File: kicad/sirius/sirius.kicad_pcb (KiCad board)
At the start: 4 copper layers, 42.1 x 65.5 mm, 60 parts, among them J1 IPEX_MHF1, J2 Power In, J3 Screw_Terminal, Q1 Q_PMOS_GSD, Q2 Q_NMOS_GSD, Q3 Q_NMOS_GSD, U1 Power_Connector, U2 AP63301WU-7, U3 RFM95W-915S2, U4 LC29H (DA), U5 Pi Zero 2W

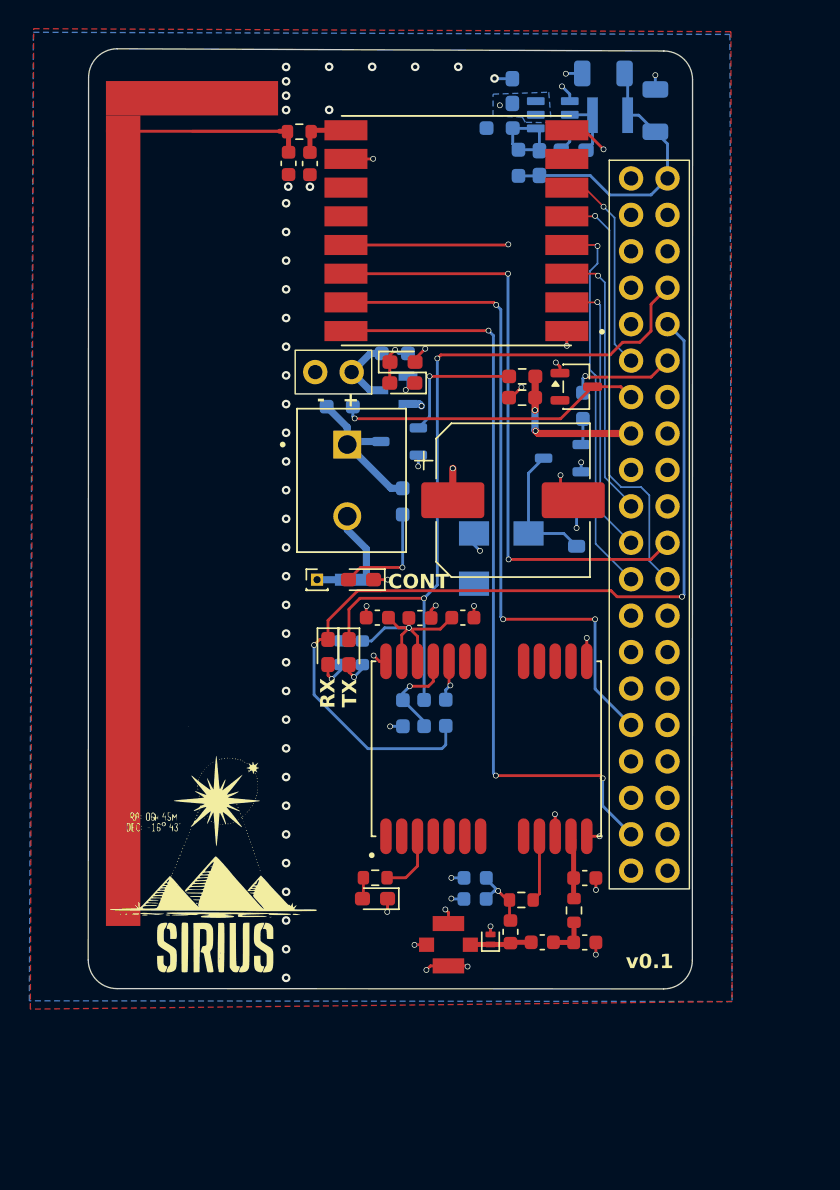
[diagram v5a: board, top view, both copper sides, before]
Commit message: WIP: Start making new version of Sirius
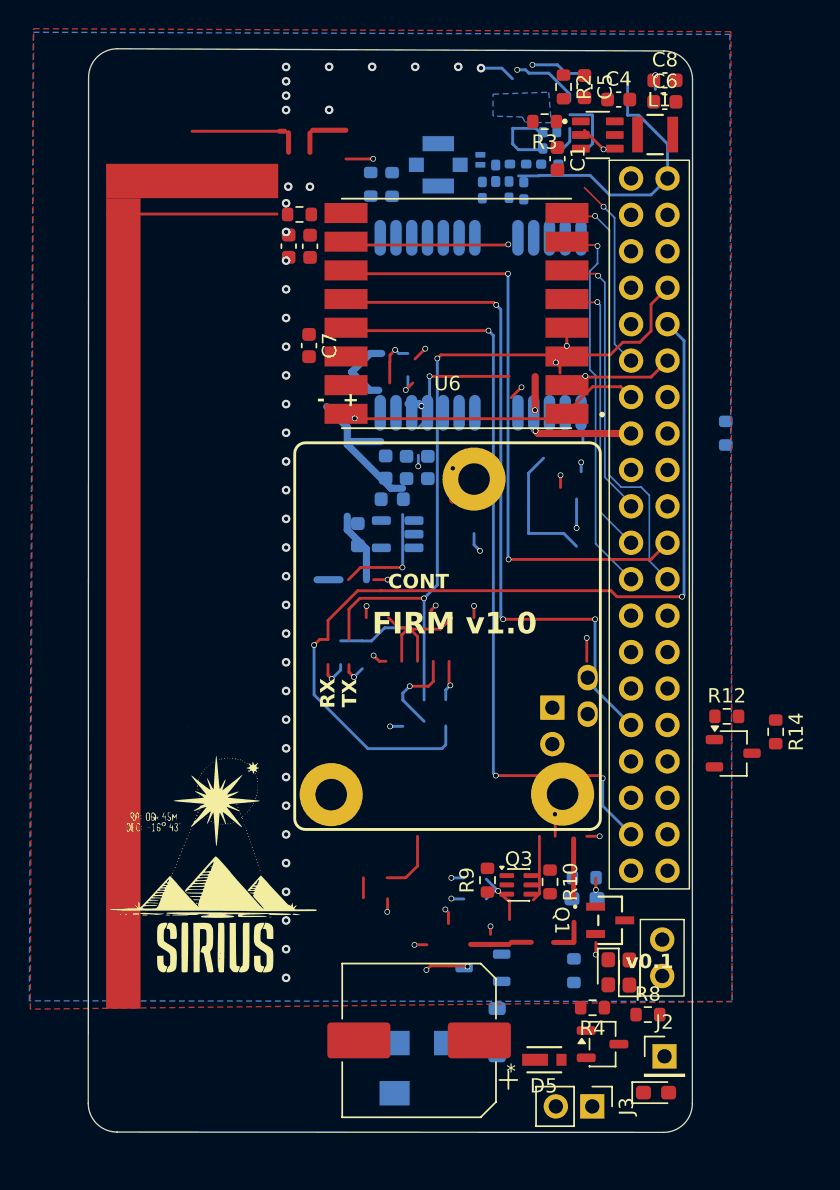
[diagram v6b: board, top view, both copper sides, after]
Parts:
- removed the D7 at (129.8, 108.4)
- removed the D8 at (131.2, 108.4)
- removed the R14 at (136.5, 112.6)
- removed the R16 at (132.2, 108.4)
- removed the R8 at (138.0, 112.6)
- added C14: 470p, Capacitor_SMD:C_0603_1608Metric, B.Cu at (131.9, 100.2)
- added C16: 10u, Capacitor_SMD:C_0603_1608Metric, B.Cu at (134.3, 97.7)
- added C8: 22u, Capacitor_SMD:C_0603_1608Metric, F.Cu at (153.3, 68.5)
- added Q3: Q_Dual_NMOS, Package_TO_SOT_SMD:SOT-363_SC-70-6, F.Cu at (143.1, 124.6)
- added R10: 10k, Resistor_SMD:R_0603_1608Metric, F.Cu at (145.3, 124.4)
- added R9: 10k, Resistor_SMD:R_0603_1608Metric, F.Cu at (140.9, 124.3)
- added U4: MIC5219-3.3YM5, Package_TO_SOT_SMD:SOT-23-5, B.Cu at (134.6, 100.1)
- added U6: ~, sirius:FIRM v1.0, F.Cu at (138.1, 107.6)
- C1, C4, C5: footprint Capacitor_SMD:C_0603_1608Metric_Pad1.08x0.95mm_HandSolder -> Capacitor_SMD:C_0603_1608Metric; moved to F.Cu
- C10: renamed from C9; footprint Capacitor_SMD:C_0603_1608Metric -> Capacitor_SMD:C_0402_1005Metric_Pad0.74x0.62mm_HandSolder; moved to B.Cu
- C11: renamed from C10; footprint Capacitor_SMD:C_0603_1608Metric -> Capacitor_SMD:C_0402_1005Metric_Pad0.74x0.62mm_HandSolder; moved to B.Cu
- C12: renamed from C11; footprint Capacitor_SMD:C_0603_1608Metric -> Capacitor_SMD:C_0402_1005Metric_Pad0.74x0.62mm_HandSolder; moved to B.Cu
- C13: renamed from C12; footprint Capacitor_SMD:C_0603_1608Metric -> Capacitor_SMD:C_0402_1005Metric_Pad0.74x0.62mm_HandSolder
- C15: renamed from C13; footprint Capacitor_SMD:C_0603_1608Metric -> Capacitor_SMD:C_0402_1005Metric_Pad0.74x0.62mm_HandSolder
- C17: renamed from C14; moved to B.Cu
- C18: renamed from C15; moved to B.Cu
- C19: renamed from C16; moved to B.Cu
- C6: footprint Capacitor_SMD:C_1206_3216Metric -> Capacitor_SMD:C_0603_1608Metric; moved to F.Cu
- C7: value 22u -> 10u; footprint Capacitor_SMD:C_1206_3216Metric -> Capacitor_SMD:C_0603_1608Metric; moved to F.Cu
- D3, J1: moved to B.Cu
- D5, L1, Q1, Q2, U2: moved to F.Cu
- D7: renamed from D9; moved to B.Cu
- J2: footprint Connector_PinHeader_1.00mm:PinHeader_1x01_P1.00mm_Vertical -> Connector_PinHeader_2.54mm:PinHeader_1x01_P2.54mm_Vertical
- J3: footprint sirius:CUI_TB002-500-02BE -> Connector_PinHeader_2.54mm:PinHeader_1x02_P2.54mm_Vertical
- L2: footprint Inductor_SMD:L_0603_1608Metric -> Inductor_SMD:L_0402_1005Metric_Pad0.77x0.64mm_HandSolder; moved to B.Cu
- R11: value 5.6k -> 12k; footprint Resistor_SMD:R_0603_1608Metric_Pad0.98x0.95mm_HandSolder -> Resistor_SMD:R_0603_1608Metric
- R12: renamed from R10; footprint Resistor_SMD:R_0603_1608Metric_Pad0.98x0.95mm_HandSolder -> Resistor_SMD:R_0603_1608Metric
- R13: renamed from R12; moved to B.Cu
- R14: renamed from R13; footprint Resistor_SMD:R_0603_1608Metric_Pad0.98x0.95mm_HandSolder -> Resistor_SMD:R_0603_1608Metric
- R15: value 1k -> 10k
- R16: renamed from R17; footprint Resistor_SMD:R_0603_1608Metric_Pad0.98x0.95mm_HandSolder -> Resistor_SMD:R_0603_1608Metric
- R2, R3, R4: footprint Resistor_SMD:R_0603_1608Metric_Pad0.98x0.95mm_HandSolder -> Resistor_SMD:R_0603_1608Metric; moved to F.Cu
- R5, R6: footprint Resistor_SMD:R_0603_1608Metric -> Resistor_SMD:R_0402_1005Metric_Pad0.72x0.64mm_HandSolder; moved to B.Cu
- R7: footprint Resistor_SMD:R_0603_1608Metric_Pad0.98x0.95mm_HandSolder -> Resistor_SMD:R_0603_1608Metric
- R8: renamed from R9; footprint Resistor_SMD:R_0603_1608Metric_Pad0.98x0.95mm_HandSolder -> Resistor_SMD:R_0603_1608Metric; moved to F.Cu
- U5: renamed from U4; moved to B.Cu
- moved C11 56.0 mm to (144.8, 72.7), turned to -90 degrees
- moved J1 54.4 mm to (137.5, 74.4), turned to 90 degrees
- moved D3 54.4 mm to (140.4, 74.0)
- moved C12 54.3 mm to (143.0, 74.3)
- moved L2 52.9 mm to (141.5, 75.0), turned to -90 degrees
- moved R5 52.1 mm to (145.2, 74.3), turned to 180 degrees
- moved C10 51.5 mm to (145.7, 72.7), turned to -90 degrees
- moved R6 49.4 mm to (143.4, 76.2), turned to -90 degrees
- moved C15 49.4 mm to (140.5, 76.2), turned to -90 degrees
- moved J3 49.2 mm to (148.2, 140.0)
- moved C13 48.0 mm to (142.4, 76.1), turned to -90 degrees
- moved R4 47.6 mm to (148.2, 133.2), turned to 180 degrees
- moved R8 47.5 mm to (152.1, 133.6), turned to 0 degrees
- moved U1 46.8 mm to (153.1, 129.7), turned to -90 degrees
- moved D6 45.9 mm to (148.9, 135.7)
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- renumbered C8 to C9, D10 to D8, Q3 to Q4, U5 to U7
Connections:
- BZ1 pad 1: +3V3 -> +3.3V
- C17 pad 2: +3V3 -> +3.3V
- C18 pad 2: +3V3 -> +3.3V
- C19 pad 2: +3V3 -> +3.3V
- C6 pad 1: +5V -> GND
- C6 pad 2: GND -> +5V
- C7 pad 1: +5V -> +3.3V
- D8 pad 1: +3V3 -> +3.3V
- R11 pad 1: /Pi_TX_2_8 -> /I2C_SELECT
- R15 pad 1: Net-(D7-A) (its old number) -> /I2C_SELECT
- R15 pad 2: +3V3 -> +3.3V
- U3 pad 13: +3V3 -> +3.3V
- U5 pad 18: unconnected-(U4-I2C_SDA/SPI_CS-Pad18) -> /SDA_2.8V
- U5 pad 19: unconnected-(U4-I2C_SCL/SPI_CLK-Pad19) -> /SCL_2.8V
- U5 pad 20: Net-(U4-TXD1) -> unconnected-(U5-TXD1-Pad20)
- U5 pad 21: /Pi_TX_2_8 -> unconnected-(U5-RXD1-Pad21)
- U5 pad 22: +3V3 -> +3.3V
- U5 pad 23: +3V3 -> +3.3V
- U5 pad 5: unconnected-(U4-D_SEL1-Pad5) -> /I2C_SELECT
- U5 pad 6: unconnected-(U4-D_SEL2-Pad6) -> /I2C_SELECT
- U5 pad 7: unconnected-(U4-VDD_EXT-Pad7) -> +2V8
- U7 pad 1: +3V3 -> unconnected-(U7-3V3_1-Pad1)
- U7 pad 17: +3V3 -> unconnected-(U7-3V3_17-Pad17)
- U7 pad 3: unconnected-(U5-GPIO2/SDA1-Pad3) -> /Pi_SDA
- U7 pad 5: unconnected-(U5-GPIO3/SCL-Pad5) -> /Pi_SCL
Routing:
- net (no net): track 0.00 -> 97.0 mm, vias 0 -> 7
- net +3V3: track 84.5 -> 0.00 mm, vias 4 -> 0
- net GND: track 35.9 -> 76.3 mm, vias 72 -> 62
- net Net-(U4-BP): track 0.00 -> 12.8 mm, vias 0 -> 1
- net VCC: track 32.1 -> 43.6 mm, vias 3 -> 2
- net /PYRO_NEGATIVE: track 10.5 -> 0.00 mm
- net Net-(Q2-G): track 9.47 -> 1.02 mm
- net Net-(D4-A): track 7.82 -> 0.00 mm, vias 1 -> 0
- net /Pi_TX_2_8: track 6.45 -> 0.00 mm, vias 1 -> 0
- net Net-(BZ1--): track 9.40 -> 3.01 mm, vias 0 -> 2
- net Net-(U2-FB): track 6.31 -> 0.00 mm
- net /PYRO_POSITIVE: track 4.98 -> 0.00 mm
- net /VDD_RF: track 4.62 -> 0.00 mm
- net /PPS: track 4.53 -> 0.00 mm
- net /Pi_SCL: track 0.00 -> 4.49 mm, vias 0 -> 1
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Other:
- board size 42.1 x 65.5 mm -> 42.1 x 75.5 mm

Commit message: Finish Sirius v0.2
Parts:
- D7, R13: moved to F.Cu
- Q1, Q3, R10, R12, R14, R9: moved to B.Cu
- moved D7 53.5 mm to (134.9, 73.6), turned to 180 degrees
- moved R13 50.6 mm to (134.9, 75.1), turned to 180 degrees
- moved R9 28.5 mm to (148.1, 96.7)
- moved Q3 27.7 mm to (145.9, 97.0), turned to 180 degrees
- moved R10 27.6 mm to (143.7, 96.8)
- moved BZ1 25.7 mm to (137.0, 111.7)
- moved Q4 25.7 mm to (141.3, 104.7)
- moved D8 25.7 mm to (142.3, 109.1)
- moved Q2 24.2 mm to (145.2, 135.9), turned to -90 degrees
- moved R14 17.1 mm to (145.8, 106.2), turned to 180 degrees
- moved R12 14.3 mm to (145.8, 104.8)
- moved R16 12.8 mm to (148.0, 101.6)
- moved R7 10.8 mm to (152.6, 139.7), turned to 0 degrees
- moved G*** 10.6 mm to (123.3, 132.1)
- moved D6 10.2 mm to (144.7, 126.4)
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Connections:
- U7 pad 11: /RESET -> unconnected-(U7-GPIO17/GPIO_GEN0-Pad11)
- U7 pad 7: unconnected-(U7-GPIO4/GPIO_GCLK-Pad7) -> /RESET
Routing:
- net (no net): track 97.0 -> 0.00 mm, vias 7 -> 0
- net +3.3V: track 3.44 -> 69.8 mm, vias 1 -> 3
- net Net-(Q2-G): track 1.02 -> 38.3 mm, vias 1 -> 3
- net VCC: track 43.6 -> 76.0 mm
- net +5V: track 26.4 -> 58.2 mm
- net /Pi_RX: track 63.3 -> 34.0 mm, vias 2 -> 0
- net /CONTINUITY_SENSE: track 21.4 -> 47.4 mm, vias 1 -> 2
- net +2V8: track 0.00 -> 22.8 mm, vias 0 -> 2
- net GND: track 76.3 -> 53.6 mm, vias 62 -> 78
- net /Pi_SDA: track 1.55 -> 23.5 mm, vias 1 -> 2
- net /Pi_SCL: track 4.49 -> 24.8 mm, vias 1 -> 2
- net /Pi_TX: track 51.0 -> 33.0 mm, vias 2 -> 1
- net /PYRO_NEGATIVE: track 0.00 -> 14.3 mm
- net /SDA_2.8V: track 0.00 -> 11.3 mm
- net Net-(U4-BP): track 12.8 -> 1.50 mm, vias 1 -> 0
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- added copper zone on In2.Cu, net GND
- added copper zone on F.Cu, net Net-(C2-Pad1)
- removed copper zone on B.Cu, net VCC
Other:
- board text added: "Designed by: Harshil M"
- board text added: "PPS"
- board text added: "v0.2"
- board text removed: "RX"
- board text removed: "TX"
- board text removed: "v0.1"
